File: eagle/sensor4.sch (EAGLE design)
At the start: 15 parts, among them X1 1503_02, X2 io, X3 1503_02

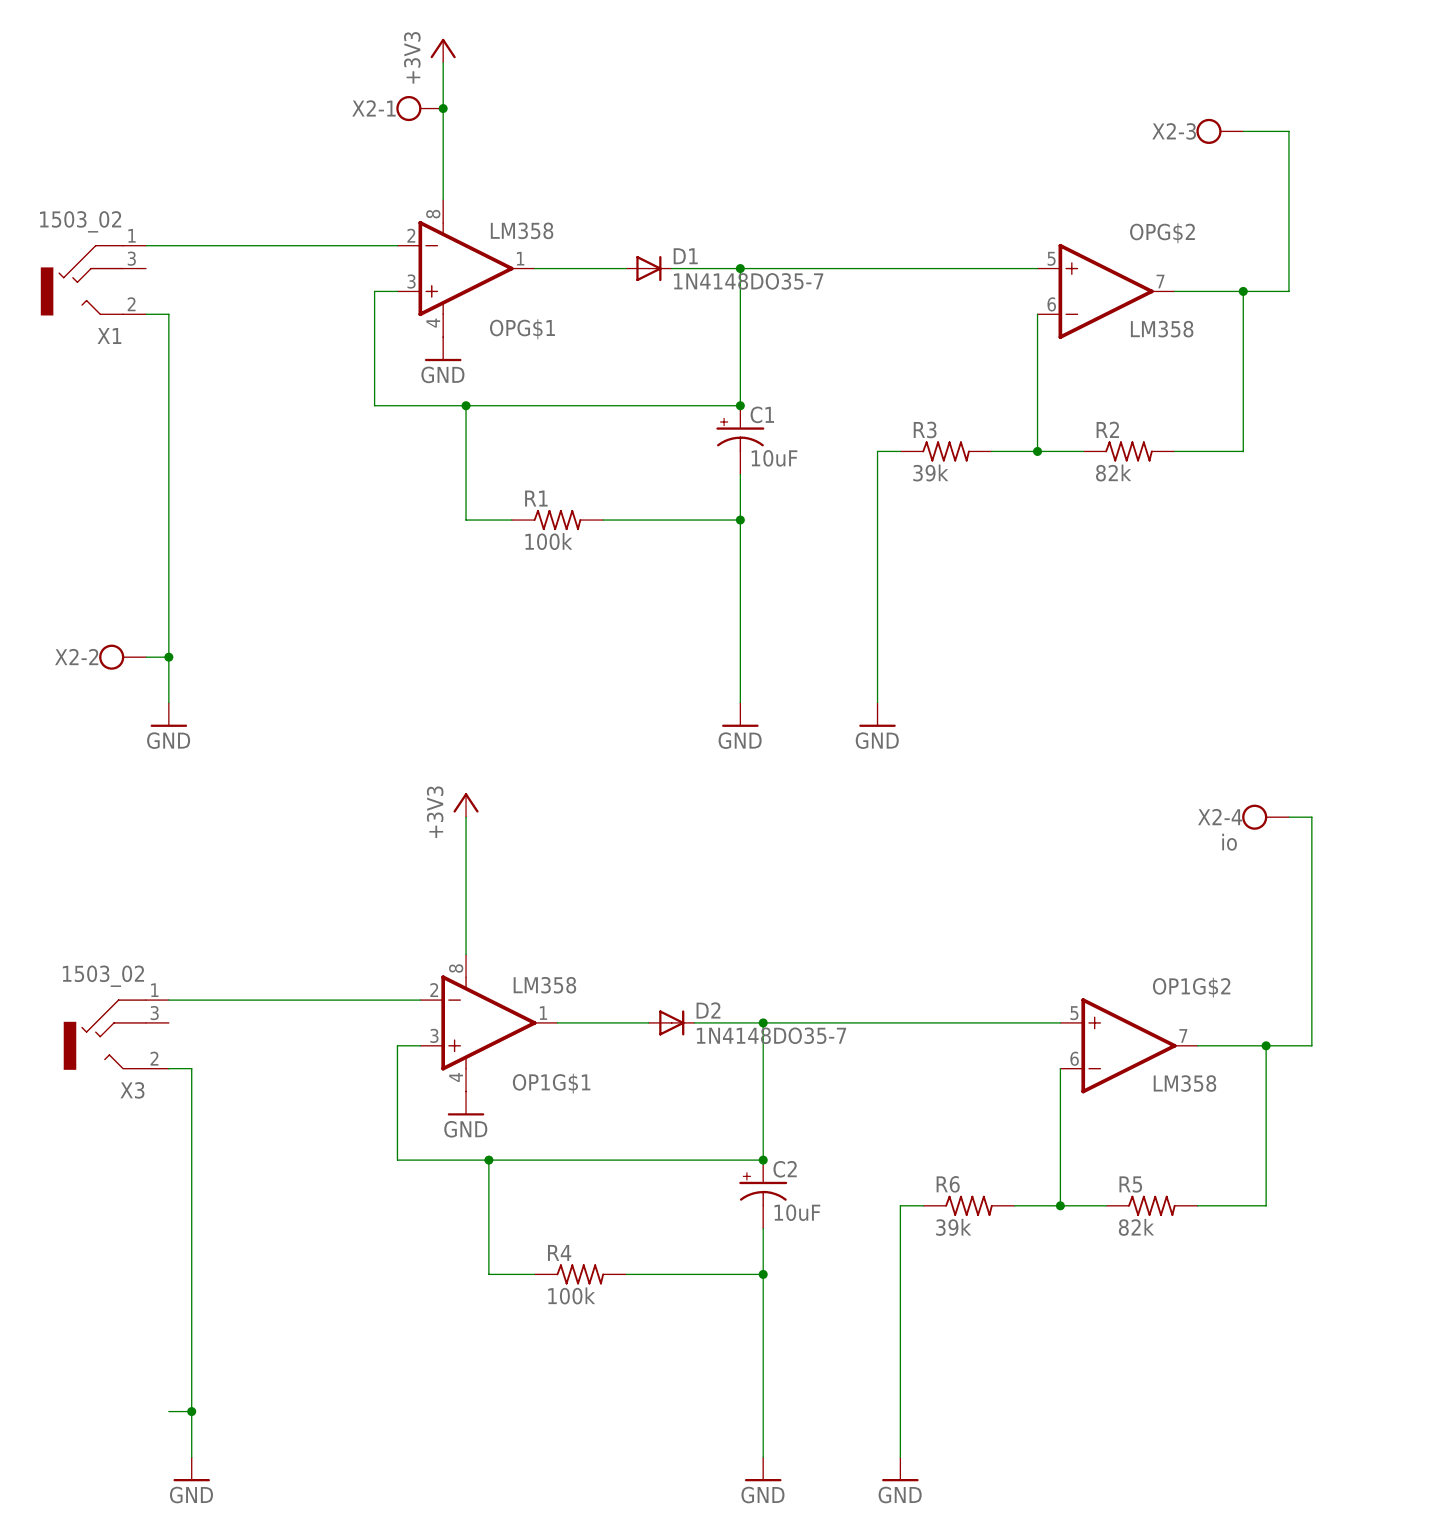
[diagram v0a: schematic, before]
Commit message: Switch to separate header pin set for signal
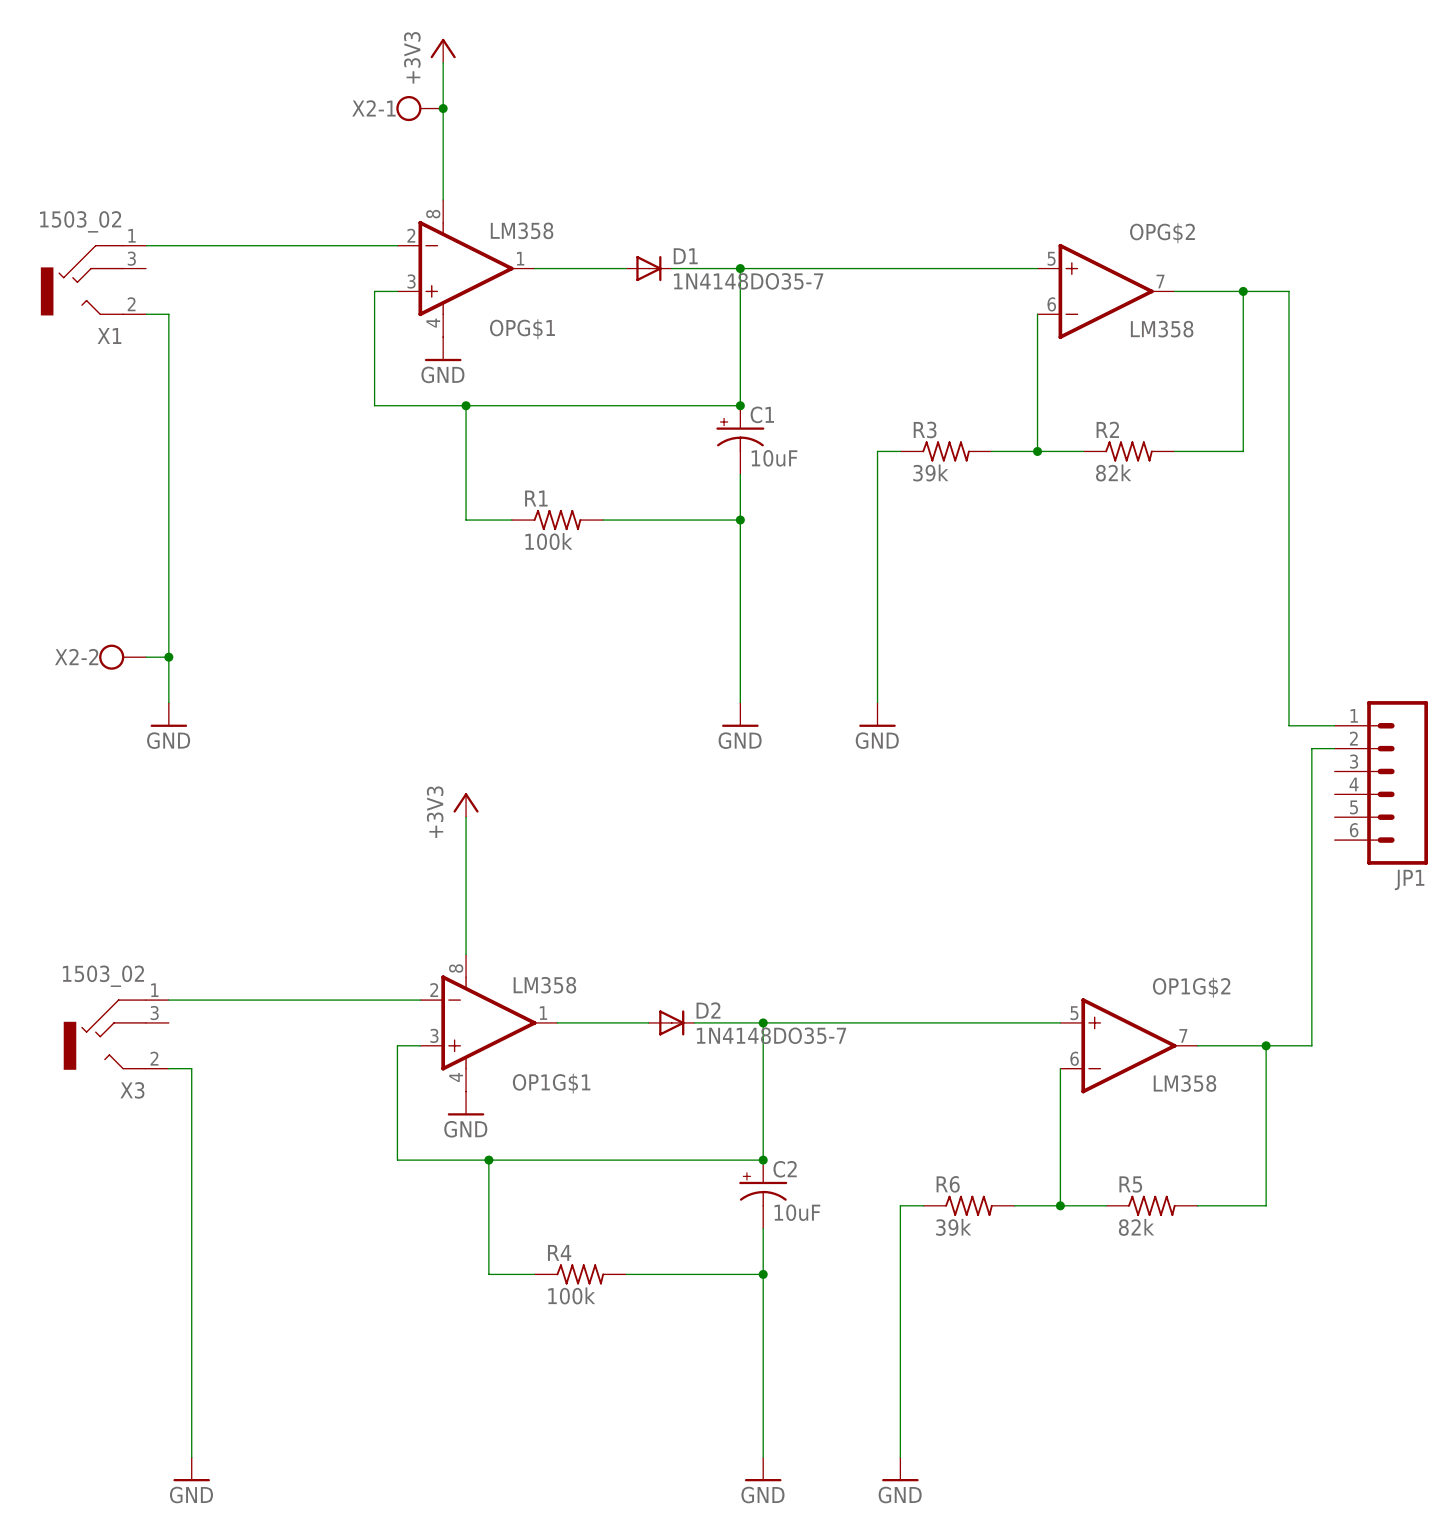
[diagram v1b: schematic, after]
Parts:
- added JP1: (no value), SparkFun-Connectors:M06SIP
- X2: value io -> (none); device con-wago-500:W237-4 -> con-wago-500:W237-102
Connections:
- net N$10: now also JP1.2; no longer X2-4.KL
- net N$7: now also JP1.1; no longer X2-3.KL
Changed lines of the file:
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@@
 <part name="GND8" library="supply1" deviceset="GND" device=""/>
 <part name="X3" library="con-lumberg" deviceset="1503_02" device=""/>
-<part name="X2" library="con-wago-500" deviceset="W237-4" device="" value="io"/>
+<part name="X2" library="con-wago-500" deviceset="W237-102" device=""/>
+<part name="JP1" library="SparkFun-Connectors" deviceset="M06" device="SIP"/>
 </parts>
 <sheets>
@@
 <instance part="X2" gate="-1" x="38.1" y="88.9"/>
 <instance part="X2" gate="-2" x="5.08" y="27.94"/>
-<instance part="X2" gate="-3" x="127" y="86.36"/>
-<instance part="X2" gate="-4" x="132.08" y="10.16"/>
+<instance part="JP1" gate="G$1" x="147.32" y="15.24" rot="R180"/>
 </instances>
 <busses>
@@
 <pinref part="GND8" gate="1" pin="GND"/>
 <wire x1="12.7" y1="-17.78" x2="15.24" y2="-17.78" width="0.1524" layer="91"/>
-<wire x1="15.24" y1="-17.78" x2="15.24" y2="-55.88" width="0.1524" layer="91"/>
+<wire x1="15.24" y1="-17.78" x2="15.24" y2="-60.96" width="0.1524" layer="91"/>
 <pinref part="X3" gate="G$1" pin="2"/>
-<wire x1="15.24" y1="-55.88" x2="15.24" y2="-60.96" width="0.1524" layer="91"/>
-<wire x1="12.7" y1="-55.88" x2="15.24" y2="-55.88" width="0.1524" layer="91"/>
-<junction x="15.24" y="-55.88"/>
 </segment>
 </net>
@@
 <junction x="132.08" y="68.58"/>
 <wire x1="132.08" y1="68.58" x2="137.16" y2="68.58" width="0.1524" layer="91"/>
-<wire x1="137.16" y1="68.58" x2="137.16" y2="86.36" width="0.1524" layer="91"/>
-<pinref part="X2" gate="-3" pin="KL"/>
-<wire x1="137.16" y1="86.36" x2="132.08" y2="86.36" width="0.1524" layer="91"/>
+<pinref part="JP1" gate="G$1" pin="1"/>
+<wire x1="142.24" y1="20.32" x2="137.16" y2="20.32" width="0.1524" layer="91"/>
+<wire x1="137.16" y1="20.32" x2="137.16" y2="68.58" width="0.1524" layer="91"/>
 </segment>
 </net>
@@
 <junction x="134.62" y="-15.24"/>
 <wire x1="134.62" y1="-15.24" x2="139.7" y2="-15.24" width="0.1524" layer="91"/>
-<pinref part="X2" gate="-4" pin="KL"/>
-<wire x1="137.16" y1="10.16" x2="139.7" y2="10.16" width="0.1524" layer="91"/>
-<wire x1="139.7" y1="10.16" x2="139.7" y2="-15.24" width="0.1524" layer="91"/>
-</segment>
-</net>
+<pinref part="JP1" gate="G$1" pin="2"/>
+<wire x1="142.24" y1="17.78" x2="139.7" y2="17.78" width="0.1524" layer="91"/>
+<wire x1="139.7" y1="17.78" x2="139.7" y2="-15.24" width="0.1524" layer="91"/>
+</segment>
+</net>
